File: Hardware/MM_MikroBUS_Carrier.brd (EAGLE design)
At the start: 80 x 35.6 mm, 88 parts, among them J15 MICROMOD-2222-C, J2 QWIIC_RIGHT_ANGLE, J5 Vertical Qwiic Connector, U1 MCP73831, U5 AP7361C-33FGEUDFN-8

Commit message: Working on proto
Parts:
- removed U$2: (no value), output:QWIIC_CARRIER_#_SINGLE0
- added U3: MIKROBUS_SMD_BLACK1, mikroBUS_SMD_BLACK:MIKROBUS_SMD_BLACK
- H5: value STAND-OFF-REFLOW2.5MM_TALL -> STAND-OFF-REFLOW-M2.5_2.5MM_TALL
- MEAS: value (none) -> JUMPER-COMBO_2_NC_TRACE
- renumbered U5 to U2
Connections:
- removed net D0: J15.10, J6.4
- removed net D1: J15.18, J6.5
- new net 5V: U3.P$10
- new net AN_IN: J15.34, U3.P$1
- new net MIK_INT: J15.10, U3.P$15
- new net MIK_RST: J15.18, U3.P$2
- new net PWM: J15.32, U3.P$16
- new net RX: J15.17, U3.P$14
- new net TX: J15.19, U3.P$13
- net 3.3V: now also U3.P$7
- net GND: now also U3.P$8, U3.P$9
- net SCL: now also TP2.1, U3.P$12; no longer TP2.P$1
- net SDA: now also TP1.1, U3.P$11; no longer TP1.P$1
- net SPI_!CS!: now also U3.P$3
- net SPI_CIPO: now also U3.P$5
- net SPI_COPI: now also U3.P$6
- net SPI_SCK: now also U3.P$4
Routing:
- net D0: track 27.1 -> 0.00 mm, vias 2 -> 0
- net D1: track 27.1 -> 0.00 mm

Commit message: Finished proto design
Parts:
- removed TP1, TP2: TEST-POINT3X5, SparkFun-Connectors:PAD.03X.05
- removed U$19: (no value), output:QWIIC_CARRIER_#_SINGLE0
- removed U$67: (no value), SparkFun-MicroMod:MICROMOD_LOGO_.5
- added U$2: (no value), SparkFun-MicroMod:MICROMOD_LOGO_.35
- moved U$44 29.2 mm to (47.2, 31.9)
- moved FD2 1.27 mm to (80.5, 34.9)
- moved FD4 1.27 mm to (80.5, 34.9)
- moved H1 1.27 mm to (78.7, 33.0)
- moved H3 1.27 mm to (78.7, 2.54)
- moved H5 0.25 mm to (44.3, 13.8)
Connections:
- net MIK_INT: now also J6.5
- net MIK_RST: now also J6.4
- net SCL: no longer TP2.1
- net SDA: no longer TP1.1
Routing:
- net MIK_INT: track 0.00 -> 87.1 mm, vias 0 -> 3
- net RX: track 0.00 -> 69.9 mm, vias 0 -> 2
- net TX: track 0.00 -> 68.9 mm, vias 0 -> 2
- net PWM: track 0.00 -> 58.6 mm, vias 0 -> 2
- net MIK_RST: track 0.00 -> 55.8 mm
- net SCL: track 28.3 -> 66.0 mm, vias 1 -> 2
- net SDA: track 29.1 -> 63.7 mm, vias 2 -> 4
- net AN_IN: track 0.00 -> 33.5 mm, vias 0 -> 2
- net SPI_CIPO: track 26.4 -> 49.2 mm, vias 1 -> 4
- net SPI_COPI: track 29.3 -> 50.4 mm, vias 1 -> 4
- net SPI_SCK: track 32.4 -> 46.7 mm, vias 1 -> 2
- net 3.3V: track 82.8 -> 93.7 mm
- net SPI_!CS!: track 34.9 -> 44.4 mm, vias 1 -> 2
- net 3.3V_EN: track 13.7 -> 16.4 mm
- net I2C_!INT!: track 27.9 -> 28.5 mm
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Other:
- board size 80 x 35.6 mm -> 81.3 x 35.6 mm
- board text added: "v01"
- board text removed: "v10"

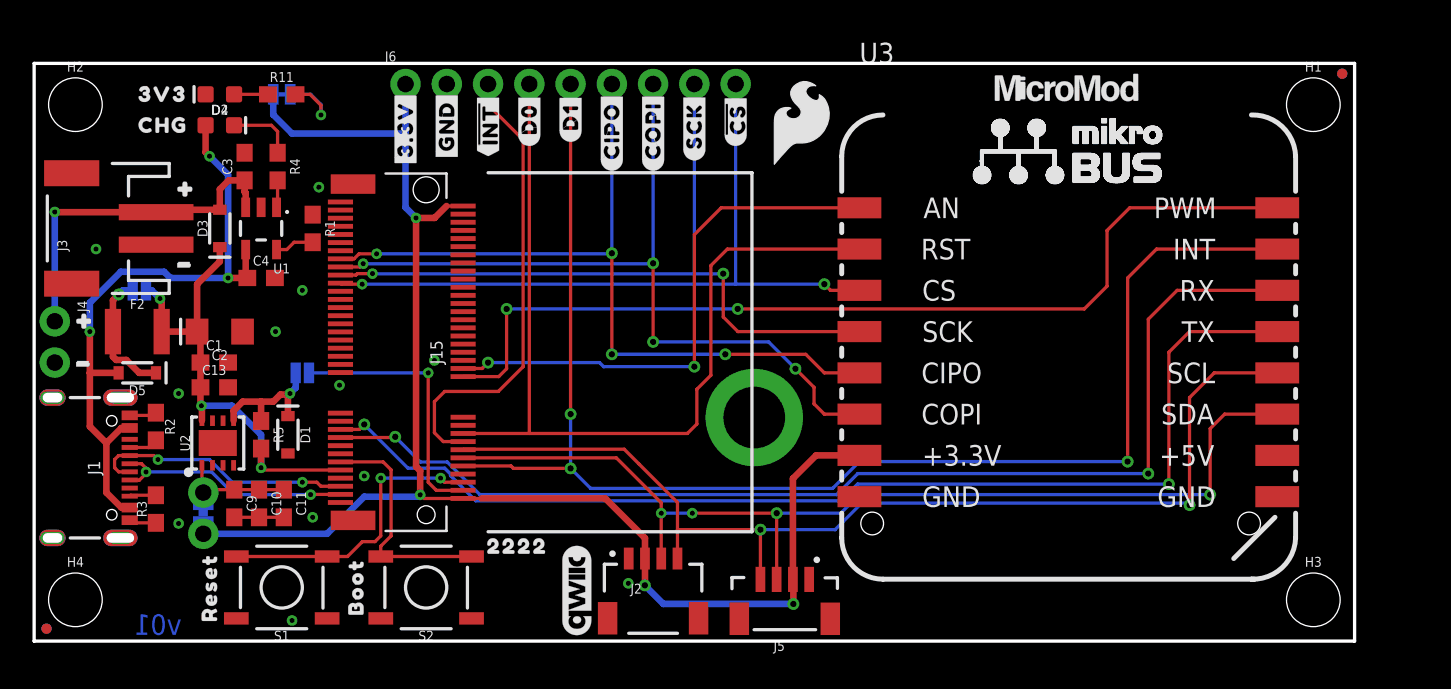
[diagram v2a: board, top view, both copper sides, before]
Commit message: Updates from proto design review
MikroBUS device:
* add pin numbers back into sch symbol
* label with a "J" prefix
* Center anchor/origin
* Remove internal pin labels
Schematic:
* 5V pin needs to be connected to "VIN" net
* Change "AN_IN" net label to "AN"
* Add a reset button for the MikroBUS
Board:
* Rotate MikroBUS 90 degrees
* More room for stand offs
* Add more GND vias
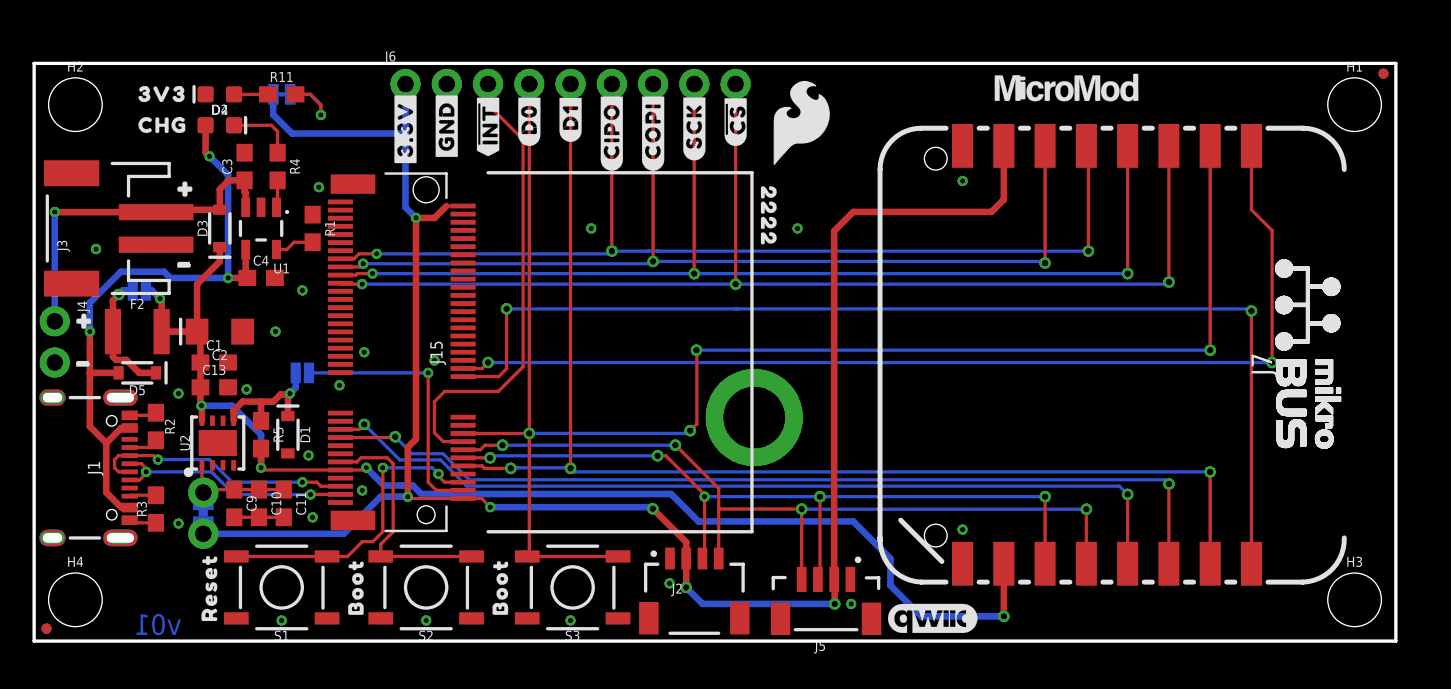
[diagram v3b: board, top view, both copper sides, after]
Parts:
- removed U3: MIKROBUS_SMD_BLACK1, mikroBUS_SMD_BLACK:MIKROBUS_SMD_BLACK
- added J7: MIKROBUS_SMD_BLACK1, mikroBUS_SMD_BLACK:MIKROBUS_SMD_BLACK
- added S3: BOOT, SparkFun-Switches:TACTILE_SWITCH_SMD_5.2MM
- added U$5: (no value), output:BOOT0
- moved U$34 29.1 mm to (45.2, 28.7), turned to 270 degrees
- moved LOGO2 22.0 mm to (55.3, 1.40), turned to 0 degrees
- moved FD2 2.54 mm to (83.1, 34.9)
- moved FD4 2.54 mm to (83.1, 34.9)
- moved H1 2.54 mm to (81.3, 33.0)
- moved H3 2.54 mm to (81.3, 2.54)
- moved J2 2.54 mm to (40.6, 5.08)
- moved J5 2.54 mm to (48.8, 4.57)
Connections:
- removed net 5V: U3.P$10
- removed net AN_IN: J15.34, U3.P$1
- new net AN: J15.34, J7.1
- net 3.3V: now also J7.7; no longer U3.P$7
- net GND: now also J7.8, J7.9, S3.1, S3.2; no longer U3.P$8, U3.P$9
- net MIK_INT: now also J7.15; no longer U3.P$15
- net MIK_RST: now also J7.2, S3.3, S3.4; no longer U3.P$2
- net PWM: now also J7.16; no longer U3.P$16
- net RX: now also J7.14; no longer U3.P$14
- net SCL: now also J7.12; no longer U3.P$12
- net SDA: now also J7.11; no longer U3.P$11
- net SPI_!CS!: now also J7.3; no longer U3.P$3
- net SPI_CIPO: now also J7.5; no longer U3.P$5
- net SPI_COPI: now also J7.6; no longer U3.P$6
- net SPI_SCK: now also J7.4; no longer U3.P$4
- net TX: now also J7.13; no longer U3.P$13
- net VIN: now also J7.10
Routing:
- net AN: track 0.00 -> 63.8 mm, vias 0 -> 2
- net VIN: track 29.3 -> 78.2 mm, vias 3 -> 5
- net MIK_RST: track 55.8 -> 98.1 mm, vias 0 -> 4
- net AN_IN: track 33.5 -> 0.00 mm, vias 2 -> 0
- net 3.3V: track 93.7 -> 121.4 mm, vias 4 -> 6
- net SPI_!CS!: track 44.4 -> 71.8 mm, vias 2 -> 3
- net SPI_SCK: track 46.7 -> 68.0 mm, vias 2 -> 3
- net SCL: track 66.0 -> 51.6 mm, vias 2 -> 4
- net TX: track 68.9 -> 54.6 mm
- net SPI_CIPO: track 49.2 -> 63.2 mm, vias 4 -> 3
- net SDA: track 63.7 -> 50.1 mm, vias 4 -> 5
- net RX: track 69.9 -> 57.1 mm
- net MIK_INT: track 87.1 -> 75.5 mm
- net SPI_COPI: track 50.4 -> 61.8 mm, vias 4 -> 3
- net PWM: track 58.6 -> 68.0 mm
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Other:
- board size 81.3 x 35.6 mm -> 83.8 x 35.6 mm

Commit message: Proto checklist
Updated silkscreen and measures
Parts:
- removed U$1: (no value), output:#3#3V_EN#0
- added U$10, U$13: (no value), output:#3V3#0
- added U$19: (no value), output:#3V3_#0
- added U$39: (no value), output:RESET0
- U$35: device output:#3#3V#0 -> output:MIKROBUS_CARRIER0
- U$38: device output:#3#3V#0 -> output:_MIKROBUS_CARRIER0
- U$5: device output:BOOT0 -> output:MIK0
- U$6: device output:#3#3V#0 -> output:#3V3_EN#0
- moved U$35 53.4 mm to (74.4, 15.1), flipped to the bottom, turned to 0 degrees
- moved U$38 44.0 mm to (57.3, 1.65), flipped to the top, turned to 0 degrees
- moved U$6 17.8 mm to (15.7, 16.5)
- moved U$2 2.57 mm to (66.0, 33.7)
- moved FD2 1.27 mm to (84.3, 34.9)
- moved FD4 1.27 mm to (84.3, 34.9)
- moved H1 1.27 mm to (82.5, 33.0)
- moved H3 1.27 mm to (82.5, 2.54)
- moved U$5 1.14 mm to (27.7, 1.40)
- moved S2 0.63 mm to (23.5, 3.30)
- moved U$31 0.51 mm to (19.3, 0.89)
- moved S1 0.38 mm to (14.9, 3.30)
- moved U$30 0.38 mm to (10.4, 0.51)
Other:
- board size 83.8 x 35.6 mm -> 85.1 x 35.6 mm

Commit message: Update schematic
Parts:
- S3: value BOOT -> MIK_RESET
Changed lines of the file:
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@@
 </element>
 <element name="U$2" library="SparkFun-MicroMod" package="MICROMOD_LOGO_.35" value="" x="66.04" y="33.655" smashed="yes"/>
-<element name="S3" library="SparkFun-Switches" package="TACTILE_SWITCH_SMD_5.2MM" value="BOOT" x="33.147" y="3.302" smashed="yes" rot="R180">
+<element name="S3" library="SparkFun-Switches" package="TACTILE_SWITCH_SMD_5.2MM" value="MIK_RESET" x="33.147" y="3.302" smashed="yes" rot="R180">
 <attribute name="NAME" x="33.147" y="0.635" size="0.6096" layer="25" font="vector" ratio="20" rot="R180" align="bottom-center"/>
 <attribute name="PROD_ID" value="SWCH-14139" x="33.147" y="3.302" size="1.778" layer="27" font="vector" ratio="15" rot="R180" display="off"/>
